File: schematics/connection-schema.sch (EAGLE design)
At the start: 7 parts

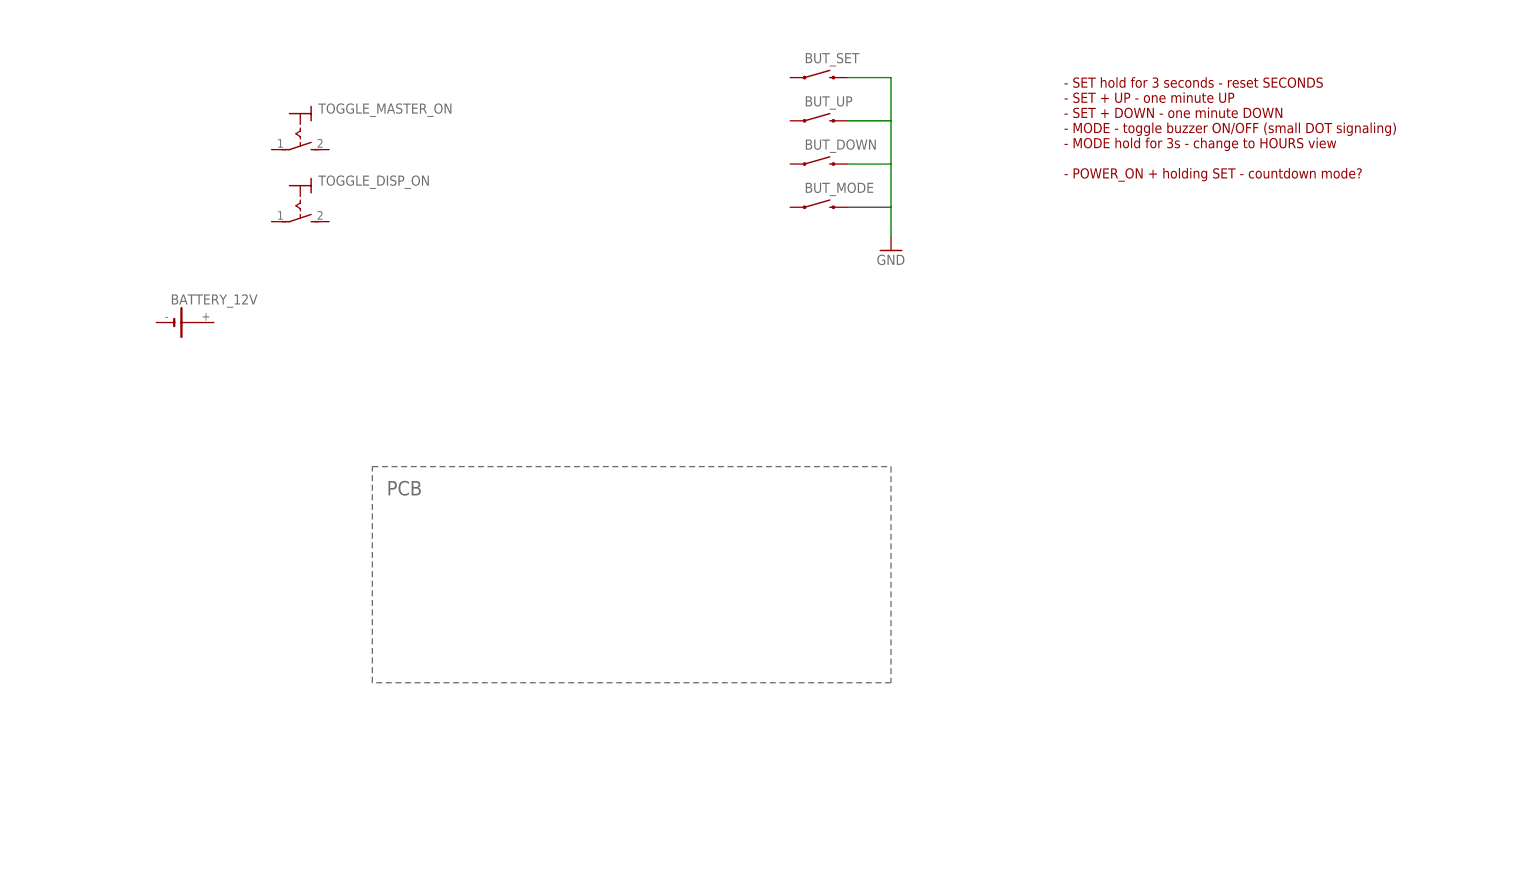
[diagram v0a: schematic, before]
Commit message: schematics: layout out-of-PCB connection schema
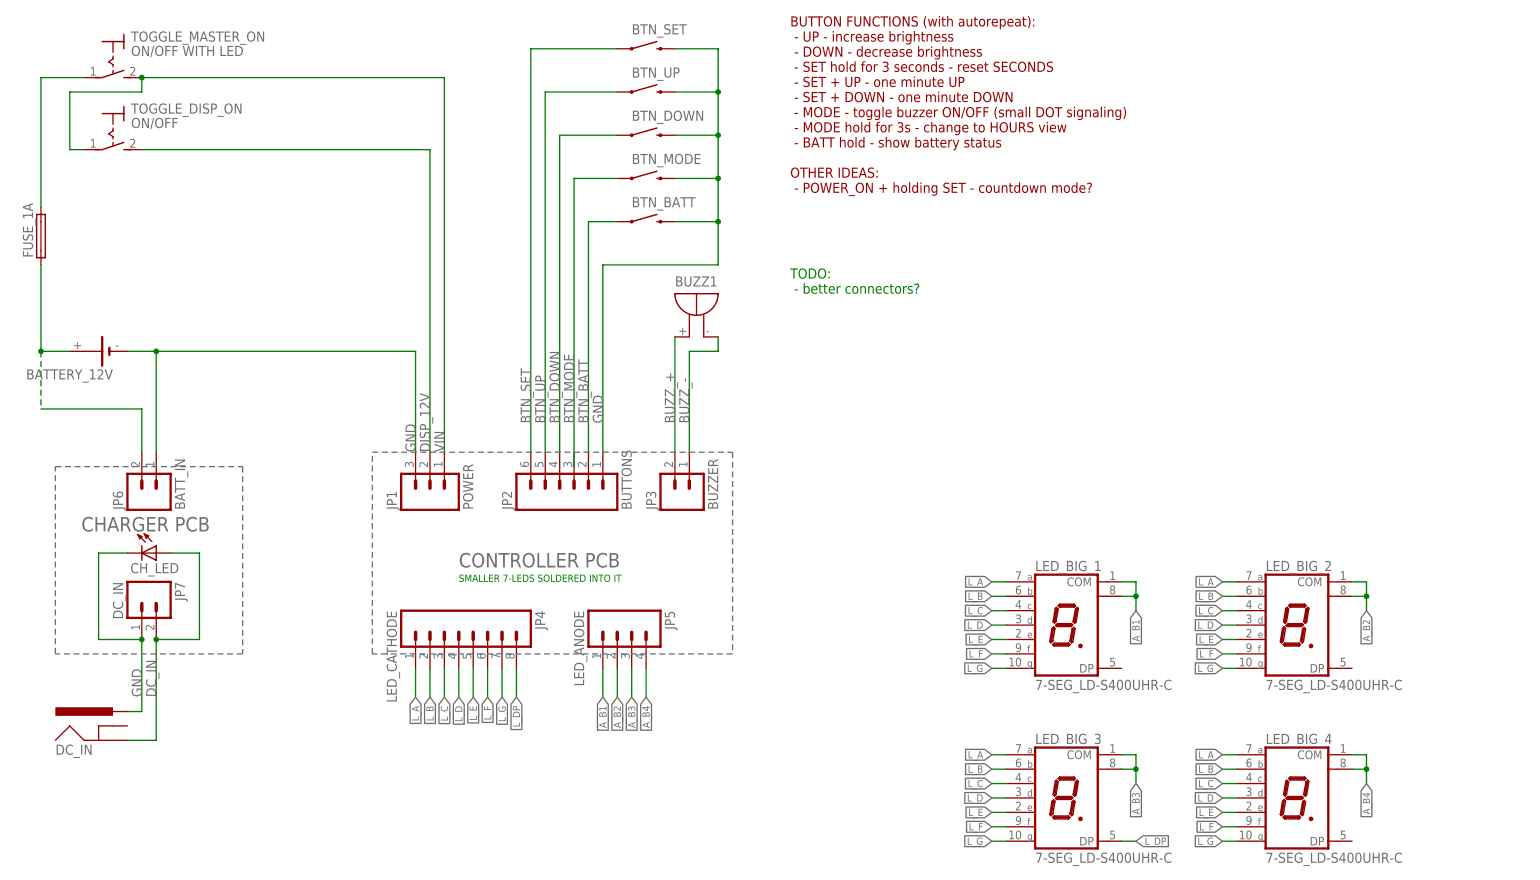
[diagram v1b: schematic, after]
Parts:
- removed BUT_DOWN, BUT_MODE, BUT_SET, BUT_UP: SWITCH-MOMENTARY-2PTH, SparkFun-Electromechanical:SWITCH-MOMENTARY-2PTH
- added BTN_BATT, BTN_DOWN, BTN_MODE, BTN_SET, BTN_UP: SWITCH-MOMENTARY-2PTH, SparkFun-Electromechanical:SWITCH-MOMENTARY-2PTH
- added BUZZ1: F/BC40, buzzer:F/BC40
- added CH_LED: (no value), led:LED5MM
- added DC_IN: POWER_JACKPTH, SparkFun-Connectors:POWER_JACKPTH
- added FUSE_1A: FUSEKS9V, fuse:FUSEKS9V
- added JP1: POWER, SparkFun-Connectors:M03POLAR
- added JP2: BUTTONS, SparkFun-Connectors:M06LONGPADS
- added JP3: BUZZER, SparkFun-Connectors:M02POLAR
- added JP4: LED_CATHODE, SparkFun-Connectors:M08
- added JP5: LED_ANODE, SparkFun-Connectors:M04PTH
- added JP6: BATT_IN, SparkFun-Connectors:M02POLAR
- added JP7: DC_IN, SparkFun-Connectors:M02POLAR
- added LED_BIG_1, LED_BIG_2, LED_BIG_3, LED_BIG_4: 7-SEG_LD-S400UHR-C, MINE:7-SEG_LD-S400UHR-C
- BATTERY_12V: value 1V60R -> 12V 7Ah
- TOGGLE_DISP_ON: value (none) -> ON/OFF
- TOGGLE_MASTER_ON: value (none) -> ON/OFF WITH LED
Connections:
- removed net N$2: BUT_UP.2
- removed net N$3: BUT_DOWN.2
- removed net N$4: BUT_MODE.2
- new net A_B1: JP5.1, LED_BIG_1.COM@1, LED_BIG_1.COM@2
- new net A_B2: JP5.2, LED_BIG_2.COM@1, LED_BIG_2.COM@2
- new net A_B3: JP5.3, LED_BIG_3.COM@1, LED_BIG_3.COM@2
- new net A_B4: JP5.4, LED_BIG_4.COM@1, LED_BIG_4.COM@2
- new net BTN_BATT: BTN_BATT.1, JP2.2
- new net BTN_DOWN: BTN_DOWN.1, JP2.4
- new net BTN_MODE: BTN_MODE.1
- new net BTN_SET: BTN_SET.1, JP2.6
- new net BTN_UP: BTN_UP.1, JP2.5
- new net BUZZ_+: BUZZ1.+, JP3.2
- new net BUZZ_-: BUZZ1.-, JP3.1
- new net DC_IN: CH_LED.A, DC_IN.GND, JP7.2
- new net DISP_12V: JP1.2, TOGGLE_DISP_ON.S
- new net L_A: JP4.1, LED_BIG_1.A, LED_BIG_2.A, LED_BIG_3.A, LED_BIG_4.A
- new net L_B: JP4.2, LED_BIG_1.B, LED_BIG_2.B, LED_BIG_3.B, LED_BIG_4.B
- new net L_C: JP4.3, LED_BIG_1.C, LED_BIG_2.C, LED_BIG_3.C, LED_BIG_4.C
- new net L_D: JP4.4, LED_BIG_1.D, LED_BIG_2.D, LED_BIG_3.D, LED_BIG_4.D
- new net L_DP: JP4.8, LED_BIG_3.DP
- new net L_E: JP4.5, LED_BIG_1.E, LED_BIG_2.E, LED_BIG_3.E, LED_BIG_4.E
- new net L_F: JP4.6, LED_BIG_1.F, LED_BIG_2.F, LED_BIG_3.F, LED_BIG_4.F
- new net L_G: JP4.7, LED_BIG_1.G, LED_BIG_2.G, LED_BIG_3.G, LED_BIG_4.G
- new net N$1: BATTERY_12V.+, FUSE_1A.1, JP6.2
- new net N$5: FUSE_1A.2, TOGGLE_MASTER_ON.P
- new net VIN: JP1.1, TOGGLE_DISP_ON.P, TOGGLE_MASTER_ON.S
- net GND: now also BATTERY_12V.-, BTN_BATT.2, BTN_DOWN.2, BTN_MODE.2, BTN_SET.2, BTN_UP.2, CH_LED.C, DC_IN.PWR, JP1.3, JP2.1, JP6.1, JP7.1; no longer BUT_SET.2
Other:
- note added: "BUTTON FUNCTIONS (with autorepeat): - UP - increase brightness - DOWN - decrease brightness - SET hold for 3 seconds - reset SECONDS - SET + UP - one minute UP - SET + DOWN - one minute DOWN - MODE - toggle buzzer ON/OFF (small DOT signaling) - MODE hold for 3s - change to HOURS view - BATT hold - show battery status OTHER IDEAS: - POWER_ON + holding SET - countdown mode?"
- note added: "CHARGER PCB"
- note added: "CONTROLLER PCB"
- note added: "SMALLER 7-LEDS SOLDERED INTO IT"
- note added: "TODO: - better connectors?"
- note removed: "- SET hold for 3 seconds - reset SECONDS - SET + UP - one minute UP - SET + DOWN - one minute DOWN - MODE - toggle buzzer ON/OFF (small DOT signaling) - MODE hold for 3s - change to HOURS view - POWER_ON + holding SET - countdown mode?"
- note removed: "PCB"
- moved on the sheet: BATTERY_12V, TOGGLE_DISP_ON, TOGGLE_MASTER_ON

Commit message: schematics: 2.0 schematics done
add: PDF printout of the 2.0 schematics
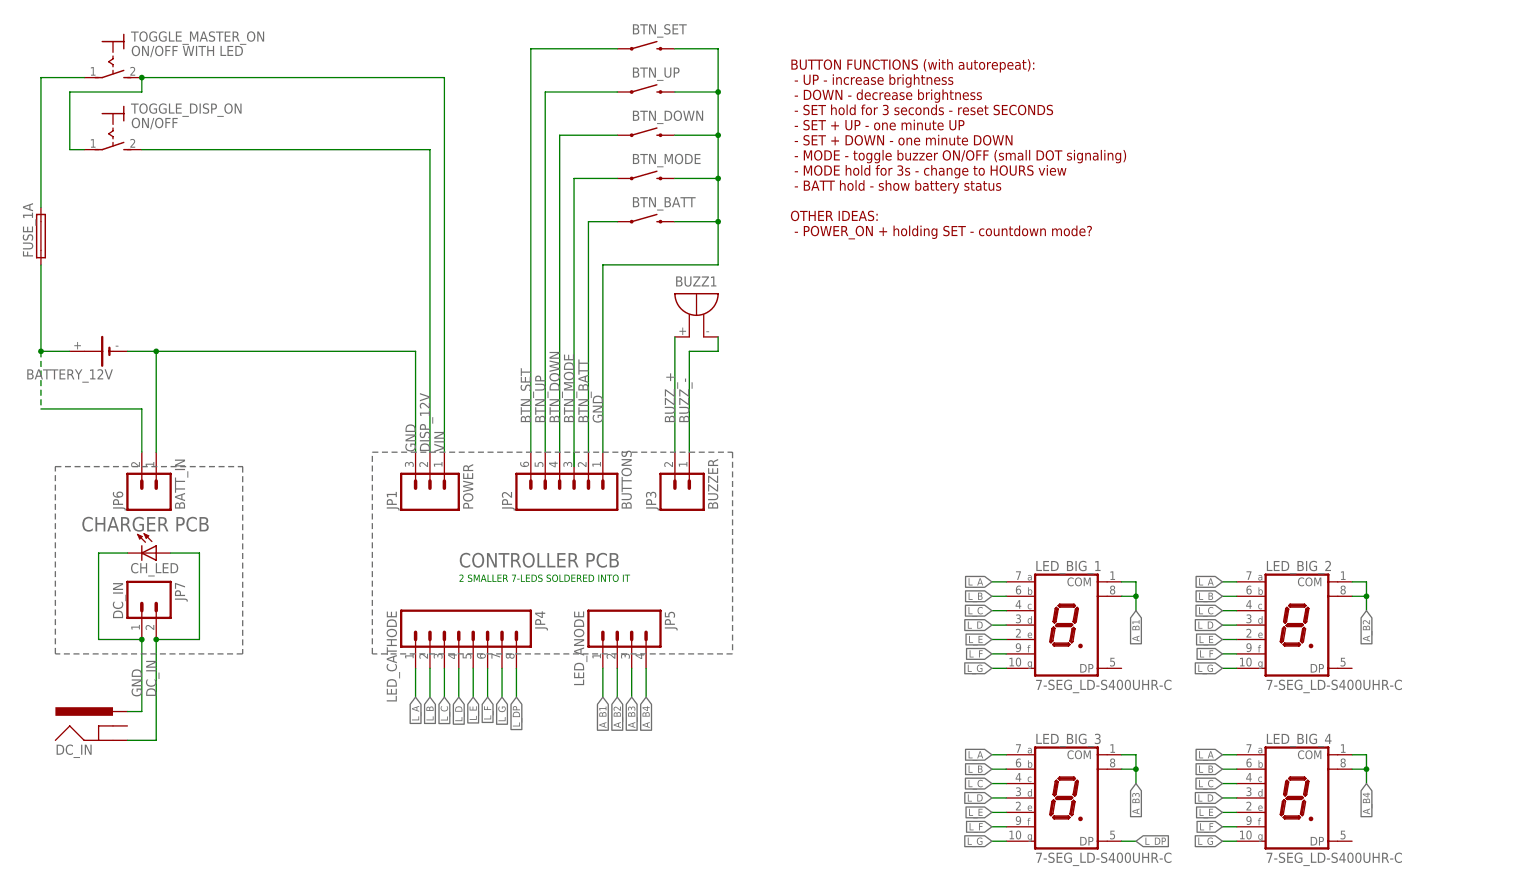
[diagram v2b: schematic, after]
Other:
- note added: "2 SMALLER 7-LEDS SOLDERED INTO IT"
- note removed: "SMALLER 7-LEDS SOLDERED INTO IT"
- note removed: "TODO: - better connectors?"
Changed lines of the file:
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@@
 <grid distance="0.1" unitdist="inch" unit="inch" style="lines" multiple="1" display="no" altdistance="0.01" altunitdist="inch" altunit="inch"/>
 <layers>
-<layer number="1" name="Top" color="4" fill="1" visible="yes" active="no"/>
-<layer number="16" name="Bottom" color="1" fill="1" visible="yes" active="no"/>
-<layer number="17" name="Pads" color="2" fill="1" visible="yes" active="no"/>
-<layer number="18" name="Vias" color="2" fill="1" visible="yes" active="no"/>
-<layer number="19" name="Unrouted" color="6" fill="1" visible="yes" active="no"/>
-<layer number="20" name="Dimension" color="15" fill="1" visible="yes" active="no"/>
-<layer number="21" name="tPlace" color="7" fill="1" visible="yes" active="no"/>
-<layer number="22" name="bPlace" color="7" fill="1" visible="yes" active="no"/>
-<layer number="23" name="tOrigins" color="15" fill="1" visible="yes" active="no"/>
-<layer number="24" name="bOrigins" color="15" fill="1" visible="yes" active="no"/>
-<layer number="25" name="tNames" color="7" fill="1" visible="yes" active="no"/>
-<layer number="26" name="bNames" color="7" fill="1" visible="yes" active="no"/>
-<layer number="27" name="tValues" color="7" fill="1" visible="yes" active="no"/>
-<layer number="28" name="bValues" color="7" fill="1" visible="yes" active="no"/>
+<layer number="1" name="Top" color="4" fill="1" visible="no" active="no"/>
+<layer number="16" name="Bottom" color="1" fill="1" visible="no" active="no"/>
+<layer number="17" name="Pads" color="2" fill="1" visible="no" active="no"/>
+<layer number="18" name="Vias" color="2" fill="1" visible="no" active="no"/>
+<layer number="19" name="Unrouted" color="6" fill="1" visible="no" active="no"/>
+<layer number="20" name="Dimension" color="15" fill="1" visible="no" active="no"/>
+<layer number="21" name="tPlace" color="7" fill="1" visible="no" active="no"/>
+<layer number="22" name="bPlace" color="7" fill="1" visible="no" active="no"/>
+<layer number="23" name="tOrigins" color="15" fill="1" visible="no" active="no"/>
+<layer number="24" name="bOrigins" color="15" fill="1" visible="no" active="no"/>
+<layer number="25" name="tNames" color="7" fill="1" visible="no" active="no"/>
+<layer number="26" name="bNames" color="7" fill="1" visible="no" active="no"/>
+<layer number="27" name="tValues" color="7" fill="1" visible="no" active="no"/>
+<layer number="28" name="bValues" color="7" fill="1" visible="no" active="no"/>
 <layer number="29" name="tStop" color="7" fill="3" visible="no" active="no"/>
 <layer number="30" name="bStop" color="7" fill="6" visible="no" active="no"/>
@@
 <layer number="35" name="tGlue" color="7" fill="4" visible="no" active="no"/>
 <layer number="36" name="bGlue" color="7" fill="5" visible="no" active="no"/>
-<layer number="37" name="tTest" color="7" fill="1" visible="yes" active="no"/>
-<layer number="38" name="bTest" color="7" fill="1" visible="yes" active="no"/>
+<layer number="37" name="tTest" color="7" fill="1" visible="no" active="no"/>
+<layer number="38" name="bTest" color="7" fill="1" visible="no" active="no"/>
 <layer number="39" name="tKeepout" color="4" fill="11" visible="no" active="no"/>
 <layer number="40" name="bKeepout" color="1" fill="11" visible="no" active="no"/>
@@
 <layer number="44" name="Drills" color="7" fill="1" visible="no" active="no"/>
 <layer number="45" name="Holes" color="7" fill="1" visible="no" active="no"/>
-<layer number="46" name="Milling" color="3" fill="1" visible="yes" active="no"/>
-<layer number="47" name="Measures" color="7" fill="1" visible="yes" active="no"/>
-<layer number="48" name="Document" color="7" fill="1" visible="yes" active="no"/>
-<layer number="49" name="Reference" color="7" fill="1" visible="yes" active="no"/>
-<layer number="50" name="dxf" color="7" fill="1" visible="yes" active="no"/>
-<layer number="51" name="tDocu" color="7" fill="1" visible="yes" active="no"/>
-<layer number="52" name="bDocu" color="7" fill="1" visible="yes" active="no"/>
-<layer number="53" name="tGND_GNDA" color="7" fill="1" visible="yes" active="no"/>
-<layer number="54" name="bGND_GNDA" color="7" fill="1" visible="yes" active="no"/>
-<layer number="56" name="wert" color="7" fill="1" visible="yes" active="no"/>
-<layer number="57" name="tCAD" color="7" fill="1" visible="yes" active="no"/>
+<layer number="46" name="Milling" color="3" fill="1" visible="no" active="no"/>
+<layer number="47" name="Measures" color="7" fill="1" visible="no" active="no"/>
+<layer number="48" name="Document" color="7" fill="1" visible="no" active="no"/>
+<layer number="49" name="Reference" color="7" fill="1" visible="no" active="no"/>
+<layer number="50" name="dxf" color="7" fill="1" visible="no" active="no"/>
+<layer number="51" name="tDocu" color="7" fill="1" visible="no" active="no"/>
+<layer number="52" name="bDocu" color="7" fill="1" visible="no" active="no"/>
+<layer number="53" name="tGND_GNDA" color="7" fill="1" visible="no" active="no"/>
+<layer number="54" name="bGND_GNDA" color="7" fill="1" visible="no" active="no"/>
+<layer number="56" name="wert" color="7" fill="1" visible="no" active="no"/>
+<layer number="57" name="tCAD" color="7" fill="1" visible="no" active="no"/>
 <layer number="90" name="Modules" color="5" fill="1" visible="yes" active="yes"/>
 <layer number="91" name="Nets" color="2" fill="1" visible="yes" active="yes"/>
@@
 <sheet>
 <plain>
-<text x="114.3" y="91.44" size="1.778" layer="94">BUTTON FUNCTIONS (with autorepeat):
+<text x="114.3" y="83.82" size="1.778" layer="94">BUTTON FUNCTIONS (with autorepeat):
  - UP - increase brightness
  - DOWN - decrease brightness
@@
 <wire x1="40.64" y1="10.16" x2="40.64" y2="45.72" width="0.1524" layer="95" style="longdash"/>
 <text x="55.88" y="25.4" size="2.54" layer="95">CONTROLLER PCB</text>
-<text x="114.3" y="73.66" size="1.778" layer="91">TODO:
- - better connectors?</text>
 <wire x1="-15.24" y1="43.18" x2="17.78" y2="43.18" width="0.1524" layer="95" style="longdash"/>
 <wire x1="17.78" y1="43.18" x2="17.78" y2="10.16" width="0.1524" layer="95" style="longdash"/>
@@
 <wire x1="-15.24" y1="10.16" x2="-15.24" y2="43.18" width="0.1524" layer="95" style="longdash"/>
 <text x="-10.668" y="31.75" size="2.54" layer="95">CHARGER PCB</text>
-<text x="55.88" y="22.86" size="1.27" layer="91">SMALLER 7-LEDS SOLDERED INTO IT</text>
+<text x="55.88" y="22.86" size="1.27" layer="91">2 SMALLER 7-LEDS SOLDERED INTO IT</text>
 </plain>
 <instances>

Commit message: schematics: finishing touches
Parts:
- JP1: value POWER -> DC_IN; device SparkFun-Connectors:M03POLAR -> SparkFun-Connectors:M03JST-PTH
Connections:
- net DISP_12V: now also JP1.3; no longer JP1.2
- net GND: now also JP1.2; no longer JP1.3
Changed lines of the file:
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@@
 <part name="LED_BIG_4" library="MINE" deviceset="7-SEG_" device="LD-S400UHR-C" value="7-SEG_LD-S400UHR-C"/>
 <part name="JP3" library="SparkFun-Connectors" deviceset="M02" device="POLAR" value="BUZZER"/>
-<part name="JP1" library="SparkFun-Connectors" deviceset="M03" device="POLAR" value="POWER"/>
+<part name="JP1" library="SparkFun-Connectors" deviceset="M03" device="JST-PTH" value="DC_IN"/>
 <part name="JP2" library="SparkFun-Connectors" deviceset="M06" device="LONGPADS" value="BUTTONS"/>
 <part name="JP4" library="SparkFun-Connectors" deviceset="M08" device="" value="LED_CATHODE"/>
@@
 <segment>
 <pinref part="TOGGLE_DISP_ON" gate="1" pin="S"/>
-<wire x1="0" y1="99.06" x2="50.8" y2="99.06" width="0.1524" layer="91"/>
-<wire x1="50.8" y1="99.06" x2="50.8" y2="45.72" width="0.1524" layer="91"/>
-<label x="50.8" y="45.72" size="1.778" layer="95" rot="R90"/>
-<pinref part="JP1" gate="G$1" pin="2"/>
+<wire x1="0" y1="99.06" x2="48.26" y2="99.06" width="0.1524" layer="91"/>
+<label x="48.26" y="45.72" size="1.778" layer="95" rot="R90"/>
+<wire x1="48.26" y1="99.06" x2="48.26" y2="45.72" width="0.1524" layer="91"/>
+<pinref part="JP1" gate="G$1" pin="3"/>
 </segment>
 </net>
@@
 <pinref part="BATTERY_12V" gate="1" pin="-"/>
 <wire x1="-2.54" y1="63.5" x2="2.54" y2="63.5" width="0.1524" layer="91"/>
-<label x="48.26" y="45.72" size="1.778" layer="95" rot="R90"/>
-<wire x1="2.54" y1="63.5" x2="48.26" y2="63.5" width="0.1524" layer="91"/>
-<wire x1="48.26" y1="63.5" x2="48.26" y2="45.72" width="0.1524" layer="91"/>
+<label x="50.8" y="45.72" size="1.778" layer="95" rot="R90"/>
+<wire x1="2.54" y1="63.5" x2="50.8" y2="63.5" width="0.1524" layer="91"/>
 <wire x1="2.54" y1="63.5" x2="2.54" y2="45.72" width="0.1524" layer="91"/>
 <junction x="2.54" y="63.5"/>
-<pinref part="JP1" gate="G$1" pin="3"/>
 <pinref part="JP6" gate="G$1" pin="1"/>
+<pinref part="JP1" gate="G$1" pin="2"/>
+<wire x1="50.8" y1="63.5" x2="50.8" y2="45.72" width="0.1524" layer="91"/>
 </segment>
 <segment>
